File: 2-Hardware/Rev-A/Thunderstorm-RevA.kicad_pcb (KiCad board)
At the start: 2 copper layers, 24 parts, among them SW1 SWITCH_SPDT, U1 M10382, U2 LM358

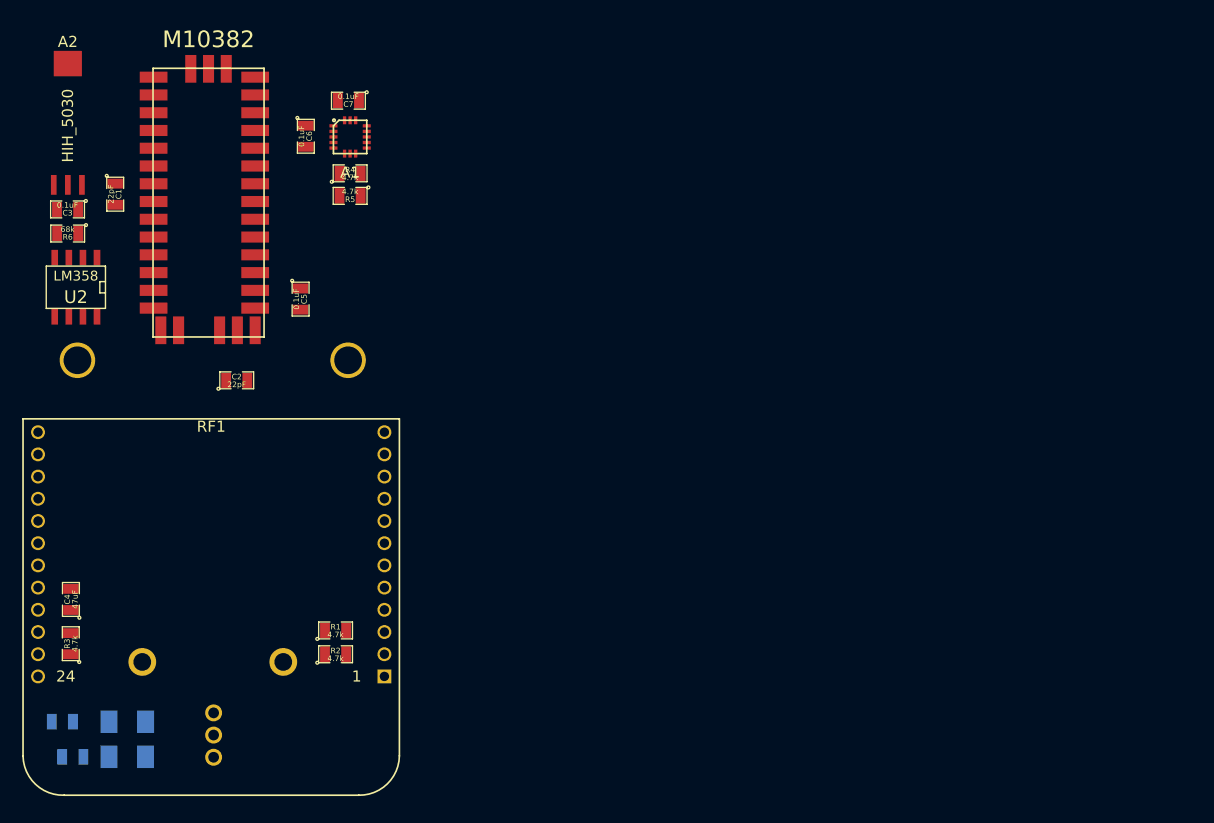
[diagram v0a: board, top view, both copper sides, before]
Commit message: Routed traces and created board outline.
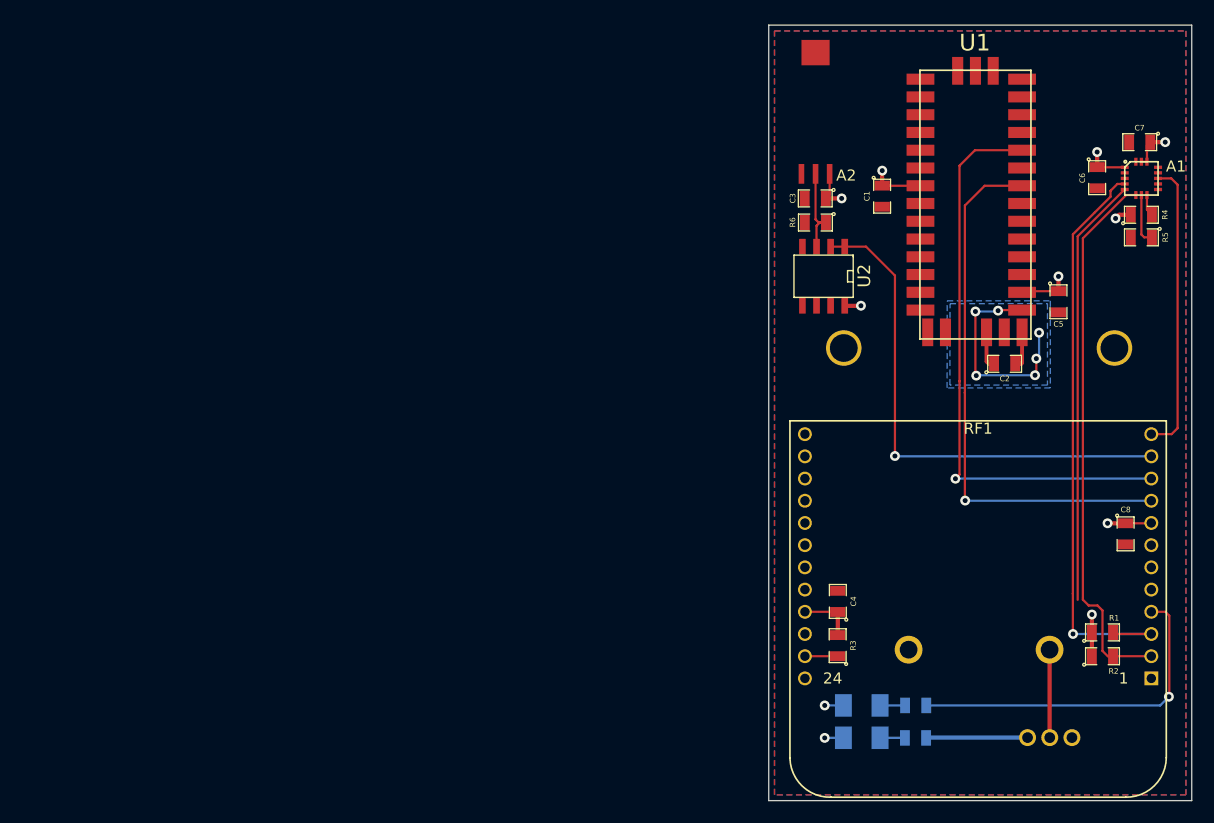
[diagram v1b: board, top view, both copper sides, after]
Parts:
- added C8: 0.1uF, SM0805, F.Cu at (202.3, 184.5)
- moved R7 76.9 mm to (183.4, 199.9), turned to 180 degrees
- moved R8 75.9 mm to (183.4, 202.9), turned to 0 degrees
- moved SW1 75.3 mm to (195.5, 202.8), turned to 0 degrees
- moved A1 71.4 mm to (203.7, 152.5)
- moved C6 71.4 mm to (199.7, 152.4)
- moved C7 71.4 mm to (203.6, 149.2)
- moved R4 71.4 mm to (203.7, 155.8)
- moved R5 71.4 mm to (203.7, 157.8)
- moved C2 69.2 mm to (191.4, 169.2)
- moved C4 69.1 mm to (176.4, 190.6)
- moved R3 69.1 mm to (176.4, 194.6)
- moved C1 69.1 mm to (180.4, 154.1)
- moved R1 69.1 mm to (200.2, 193.4)
- moved R2 69.1 mm to (200.2, 195.5)
- moved U1 69.1 mm to (188.8, 154.8)
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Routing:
- net GND: track 0.00 -> 61.5 mm, vias 0 -> 8
- net /SCL: track 0.00 -> 53.4 mm, vias 0 -> 1
- net /USART_RF_TXO: track 0.00 -> 52.2 mm, vias 0 -> 1
- net /SDA: track 0.00 -> 49.3 mm
- net /USART_RF_RXI: track 0.00 -> 49.3 mm, vias 0 -> 1
- net +BATT: track 0.00 -> 46.5 mm, vias 0 -> 9
- net /ADC3: track 0.00 -> 46.2 mm, vias 0 -> 1
- net N-0000012: track 0.00 -> 31.3 mm, vias 0 -> 1
- net /Data_Ready: track 0.00 -> 26.5 mm
- net N-0000028: track 0.00 -> 7.93 mm
- net N-0000011: track 0.00 -> 7.45 mm
- net N-000002: track 0.00 -> 4.61 mm
- net N-000009: track 0.00 -> 3.41 mm
- net N-0000010: track 0.00 -> 3.39 mm
- net N-0000018: track 0.00 -> 2.95 mm
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- added copper zone on B.Cu, net +BATT
- added copper zone on B.Cu, net GND
- added copper zone on F.Cu, net GND
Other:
- board outline added: 38.1 x 69.8 mm
- net class 50ohm added: clearance 0.254, trace_width 0.349, via_dia 0.889, via_drill 0.635
- net class Default: clearance 0.254 -> 0.2032; trace_width 0.254 -> 0.2032
- net class Power added: clearance 0.2032, trace_width 0.381, via_dia 0.889, via_drill 0.635
- rule trace_clearance: 0.254 -> 0.2032
- rule trace_min: 0.254 -> 0.1524
